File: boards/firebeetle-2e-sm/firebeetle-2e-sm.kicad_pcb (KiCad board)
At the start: 2 copper layers, 61 x 48.3 mm, 17 parts, among them J1 Power In, J2 Wiegand, J3 Feedback, J4 Button, J5 Relay, M1 MountingHole_2.2mm_M2_DIN965_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, M2 MountingHole_2.2mm_M2_DIN965_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, M3 MountingHole_2.2mm_M2_DIN965_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, M4 MountingHole_2.2mm_M2_DIN965_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, U1 DFR0654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

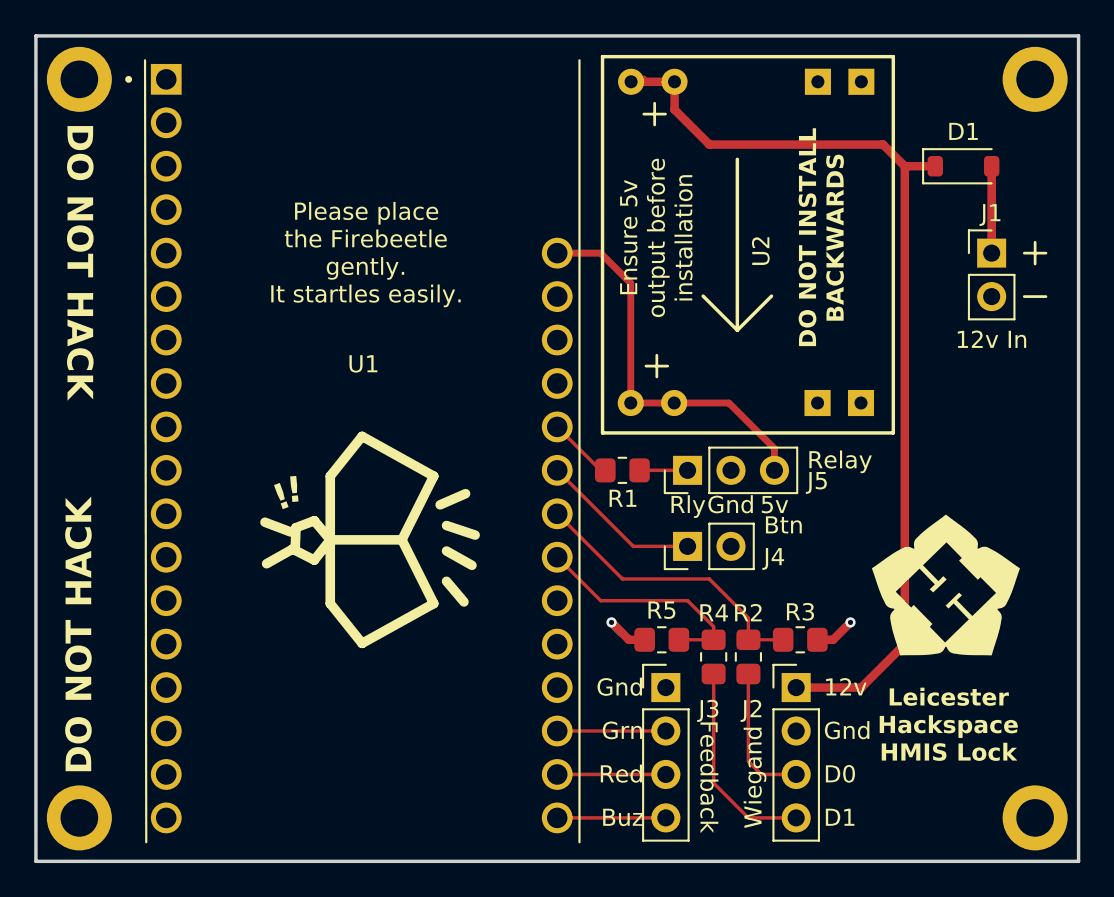
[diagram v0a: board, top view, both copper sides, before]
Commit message: Addressed design rules for firebeetle surface mount
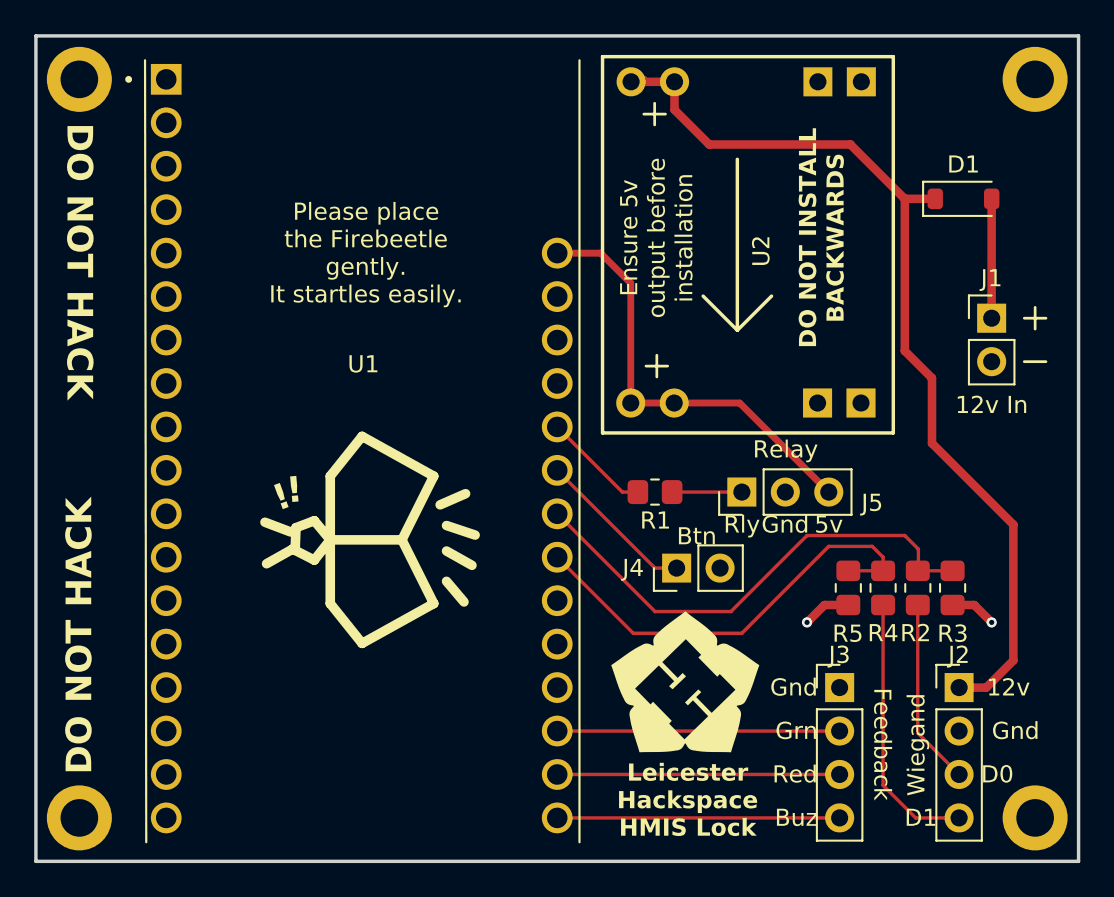
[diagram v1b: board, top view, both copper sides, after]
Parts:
- moved R5 11.3 mm to (75.4, 65.3), turned to -90 degrees
- moved R4 10.7 mm to (77.5, 65.3)
- moved R2 10.7 mm to (79.5, 65.3)
- moved J3 10.2 mm to (74.9, 71.1)
- moved J2 9.53 mm to (81.9, 71.1)
- moved R3 9.41 mm to (81.5, 65.3), turned to 90 degrees
- moved J1 3.80 mm to (83.8, 49.5)
- moved J5 3.42 mm to (69.2, 59.7)
- moved R1 2.29 mm to (64.1, 59.7)
- moved D1 1.91 mm to (82.2, 42.5)
- moved J4 1.42 mm to (65.4, 64.1)
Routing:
- net /d1: track 13.6 -> 26.1 mm
- net /d0: track 17.0 -> 29.0 mm
- net /red: track 6.35 -> 16.5 mm
- net /grn: track 6.35 -> 16.5 mm
- net /buz: track 6.35 -> 16.5 mm
- net Net-(J2-Pin_4): track 12.0 -> 15.8 mm
- net +5V: track 22.8 -> 25.8 mm
- net Net-(J2-Pin_3): track 8.22 -> 10.9 mm
- net /Relay: track 3.86 -> 6.29 mm
- net Net-(D1-A): track 5.08 -> 6.98 mm
- net Net-(J5-Pin_1): track 2.81 -> 4.08 mm
- net +12V: track 56.2 -> 55.1 mm

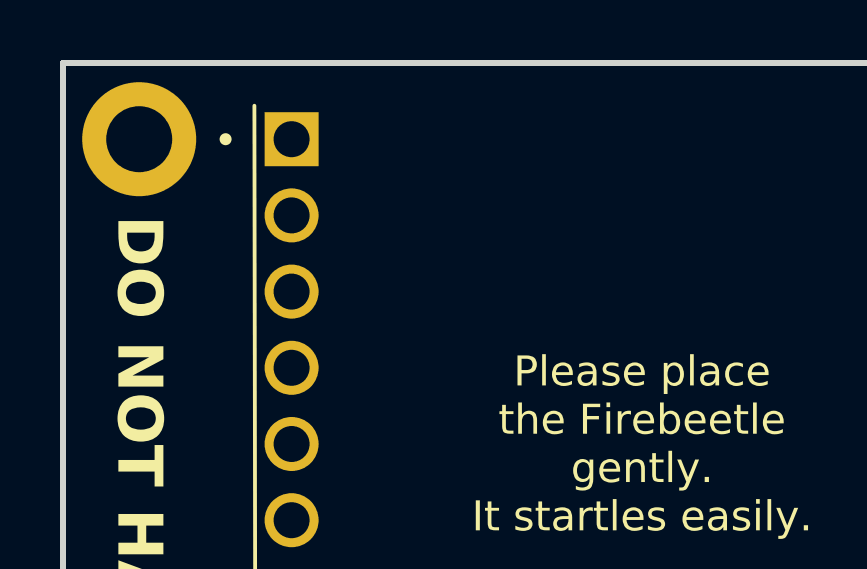
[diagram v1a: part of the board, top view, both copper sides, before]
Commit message: Added 10uF capacitor between reset and ground to handle slow power supply
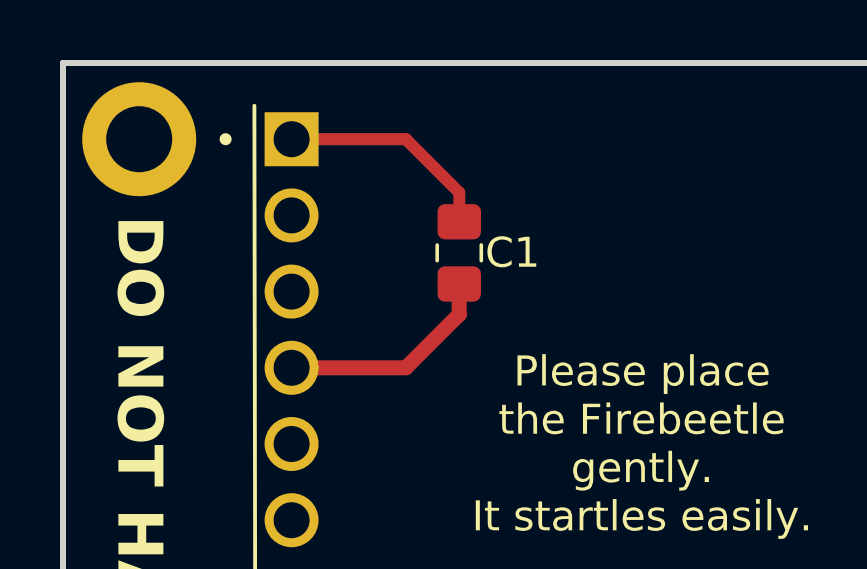
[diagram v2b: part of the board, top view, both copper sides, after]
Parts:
- added C1: 10uF, Capacitor_SMD:C_0805_2012Metric_Pad1.18x1.45mm_HandSolder, F.Cu at (41.1, 39.3)
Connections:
- U1 pad 9: unconnected-(U1-RESET-Pad9) -> Net-(U1-RESET)
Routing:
- net GND: track 5.54 -> 12.9 mm
- net Net-(U1-RESET): track 0.00 -> 7.30 mm
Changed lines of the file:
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@@
 	(net 18 "unconnected-(U1-D5-Pad0)")
 	(net 19 "unconnected-(U1-MISO-Pad19)")
-	(net 20 "unconnected-(U1-RESET-Pad9)")
+	(net 20 "Net-(U1-RESET)")
 	(net 21 "unconnected-(U1-TX-Pad1)")
 	(net 22 "unconnected-(U1-D13-Pad12)")
@@
 		)
 	)
+	(footprint "Capacitor_SMD:C_0805_2012Metric_Pad1.18x1.45mm_HandSolder"
+		(layer "F.Cu")
+		(at 41.148 39.3485 90)
+		(descr "Capacitor SMD 0805 (2012 Metric), square (rectangular) end terminal, IPC_7351 nominal with elongated pad for handsoldering. (Body size source: IPC-SM-782 page 76, https://www.pcb-3d.com/wordpress/wp-content/uploads/ipc-sm-782a_amendment_1_and_2.pdf, https://docs.google.com/spreadsheets/d/1BsfQQcO9C6DZCsRaXUlFlo91Tg2WpOkGARC1WS5S8t0/edit?usp=sharing), generated with kicad-footprint-generator")
+		(tags "capacitor handsolder")
+		(property "Reference" "C1"
+			(at 0 1.778 180)
+			(layer "F.SilkS")
+			(effects
+				(font
+					(size 1 1)
+					(thickness 0.15)
+				)
+			)
+		)
+		(property "Value" "10uF"
+			(at 0 1.68 90)
+			(layer "F.Fab")
+			(hide yes)
+			(effects
+				(font
+					(size 1 1)
+					(thickness 0.15)
+				)
+			)
+		)
+		(property "Datasheet" ""
+			(at 0 0 90)
+			(unlocked yes)
+			(layer "F.Fab")
+			(hide yes)
+			(effects
+				(font
+					(size 1.27 1.27)
+					(thickness 0.15)
+				)
+			)
+		)
+		(property "Description" "Unpolarized capacitor"
+			(at 0 0 90)
+			(unlocked yes)
+			(layer "F.Fab")
+			(hide yes)
+			(effects
+				(font
+					(size 1.27 1.27)
+					(thickness 0.15)
+				)
+			)
+		)
+		(property ki_fp_filters "C_*")
+		(sheetname "/")
+		(sheetfile "firebeetle-2e-sm.kicad_sch")
+		(attr smd)
+		(fp_line
+			(start -0.261252 -0.735)
+			(end 0.261252 -0.735)
+			(stroke
+				(width 0.12)
+				(type solid)
+			)
+			(layer "F.SilkS")
+		)
+		(fp_line
+			(start -0.261252 0.735)
+			(end 0.261252 0.735)
+			(stroke
+				(width 0.12)
+				(type solid)
+			)
+			(layer "F.SilkS")
+		)
+		(fp_line
+			(start 1.88 -0.98)
+			(end 1.88 0.98)
+			(stroke
+				(width 0.05)
+				(type solid)
+			)
+			(layer "F.CrtYd")
+		)
+		(fp_line
+			(start -1.88 -0.98)
+			(end 1.88 -0.98)
+			(stroke
+				(width 0.05)
+				(type solid)
+			)
+			(layer "F.CrtYd")
+		)
+		(fp_line
+			(start 1.88 0.98)
+			(end -1.88 0.98)
+			(stroke
+				(width 0.05)
+				(type solid)
+			)
+			(layer "F.CrtYd")
+		)
+		(fp_line
+			(start -1.88 0.98)
+			(end -1.88 -0.98)
+			(stroke
+				(width 0.05)
+				(type solid)
+			)
+			(layer "F.CrtYd")
+		)
+		(fp_line
+			(start 1 -0.625)
+			(end 1 0.625)
+			(stroke
+				(width 0.1)
+				(type solid)
+			)
+			(layer "F.Fab")
+		)
+		(fp_line
+			(start -1 -0.625)
+			(end 1 -0.625)
+			(stroke
+				(width 0.1)
+				(type solid)
+			)
+			(layer "F.Fab")
+		)
+		(fp_line
+			(start 1 0.625)
+			(end -1 0.625)
+			(stroke
+				(width 0.1)
+				(type solid)
+			)
+			(layer "F.Fab")
+		)
+		(fp_line
+			(start -1 0.625)
+			(end -1 -0.625)
+			(stroke
+				(width 0.1)
+				(type solid)
+			)
+			(layer "F.Fab")
+		)
+		(fp_text user "${REFERENCE}"
+			(at 0 0 90)
+			(layer "F.Fab")
+			(effects
+				(font
+					(size 0.5 0.5)
+					(thickness 0.08)
+				)
+			)
+		)
+		(pad "1" smd roundrect
+			(at -1.0375 0 90)
+			(size 1.175 1.45)
+			(layers "F.Cu" "F.Mask" "F.Paste")
+			(roundrect_rratio 0.212766)
+			(net 1 "GND")
+			(pintype "passive")
+		)
+		(pad "2" smd roundrect
+			(at 1.0375 0 90)
+			(size 1.175 1.45)
+			(layers "F.Cu" "F.Mask" "F.Paste")
+			(roundrect_rratio 0.212766)
+			(net 20 "Net-(U1-RESET)")
+			(pintype "passive")
+		)
+		(embedded_fonts no)
+		(model "${KICAD9_3DMODEL_DIR}/Capacitor_SMD.3dshapes/C_0805_2012Metric.wrl"
+			(offset
+				(xyz 0 0 0)
+			)
+			(scale
+				(xyz 1 1 1)
+			)
+			(rotate
+				(xyz 0 0 0)
+			)
+		)
+	)
 	(footprint "Connector_PinHeader_2.54mm:PinHeader_1x02_P2.54mm_Vertical"
 		(layer "F.Cu")
@@
 			(layers "*.Cu" "*.Mask")
 			(remove_unused_layers no)
-			(net 20 "unconnected-(U1-RESET-Pad9)")
+			(net 20 "Net-(U1-RESET)")
 			(pinfunction "RESET")
-			(pintype "input+no_connect")
+			(pintype "input")
 			(solder_mask_margin 0.102)
 		)
@@
 	)
 	(segment
+		(start 41.148 41.402)
+		(end 41.148 40.386)
+		(width 0.5)
+		(layer "F.Cu")
+		(net 1)
+	)
+	(segment
+		(start 39.37 43.18)
+		(end 41.148 41.402)
+		(width 0.5)
+		(layer "F.Cu")
+		(net 1)
+	)
+	(segment
 		(start 82.804 66.294)
 		(end 83.82 67.31)
@@
 	)
 	(segment
+		(start 35.56 43.18)
+		(end 39.37 43.18)
+		(width 0.5)
+		(layer "F.Cu")
+		(net 1)
+	)
+	(segment
 		(start 81.534 66.294)
 		(end 82.804 66.294)
@@
 	)
 	(segment
+		(start 39.37 35.56)
+		(end 41.148 37.338)
+		(width 0.4)
+		(layer "F.Cu")
+		(net 20)
+	)
+	(segment
+		(start 35.56 35.56)
+		(end 39.37 35.56)
+		(width 0.4)
+		(layer "F.Cu")
+		(net 20)
+	)
+	(segment
+		(start 41.148 37.338)
+		(end 41.148 38.311)
+		(width 0.4)
+		(layer "F.Cu")
+		(net 20)
+	)
+	(segment

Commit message: Revert EN capacitor, update firebeetle th, updated documentation to remove MP2307EN SS capacitor
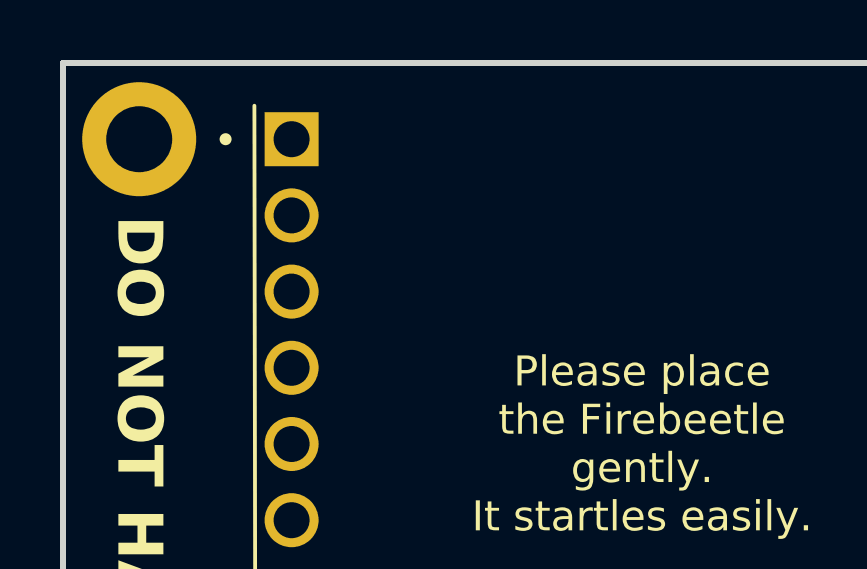
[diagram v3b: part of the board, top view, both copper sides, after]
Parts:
- removed C1: 10uF, Capacitor_SMD:C_0805_2012Metric_Pad1.18x1.45mm_HandSolder
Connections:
- U1 pad 9: Net-(U1-RESET) -> unconnected-(U1-RESET-Pad9)
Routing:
- net GND: track 12.9 -> 5.54 mm
- net Net-(U1-RESET): track 7.30 -> 0.00 mm
